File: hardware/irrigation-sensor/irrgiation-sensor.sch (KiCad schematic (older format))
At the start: 35 parts, among them J1 CONUFL001-SMD-T, J2 SHF-105-01-L-D-TH, Q1 PMV250EPEA, Q2 TSM260P02, U1 24LC32, U2 RFM95W, U3 TLV61225, U4 STM32L412KB

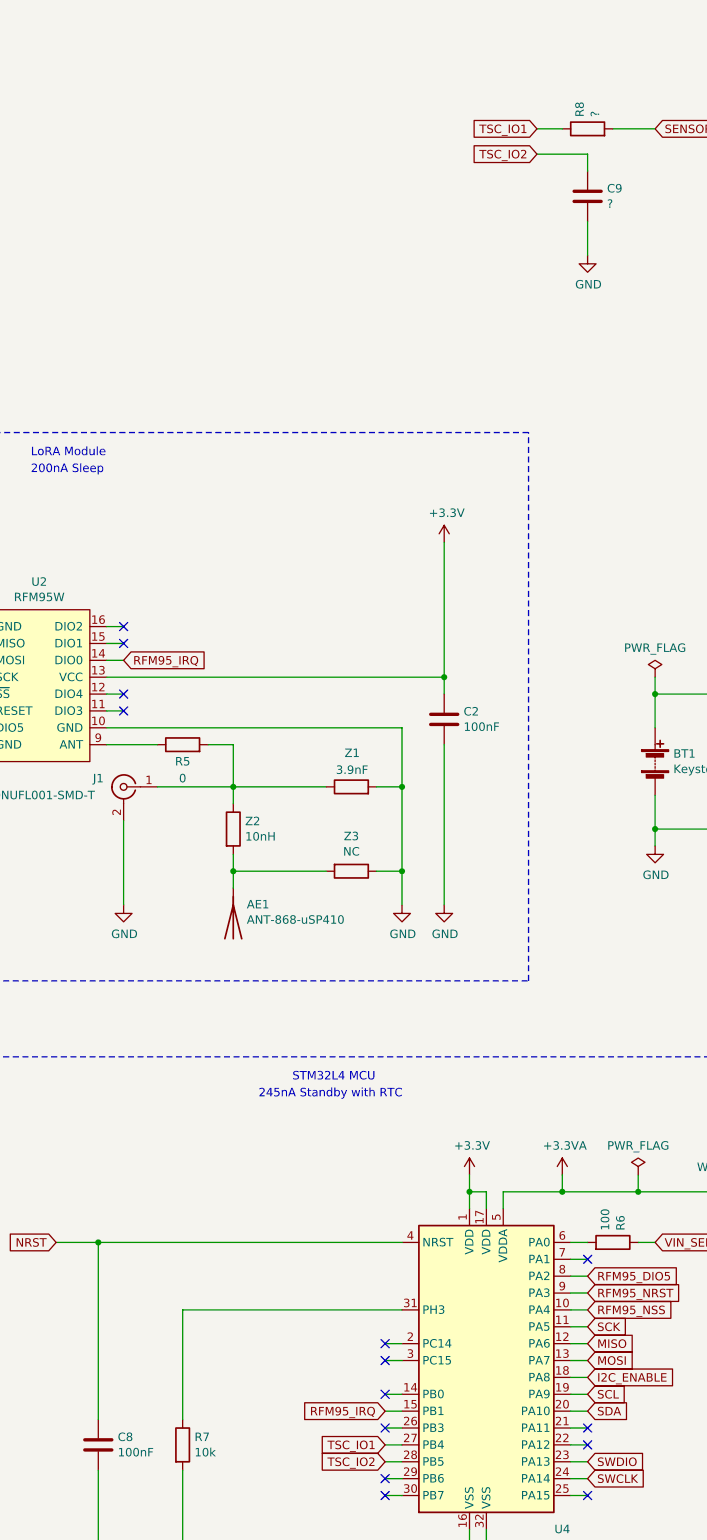
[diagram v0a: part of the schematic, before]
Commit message: PCB revision 2, add data packet handling to climate-sensor
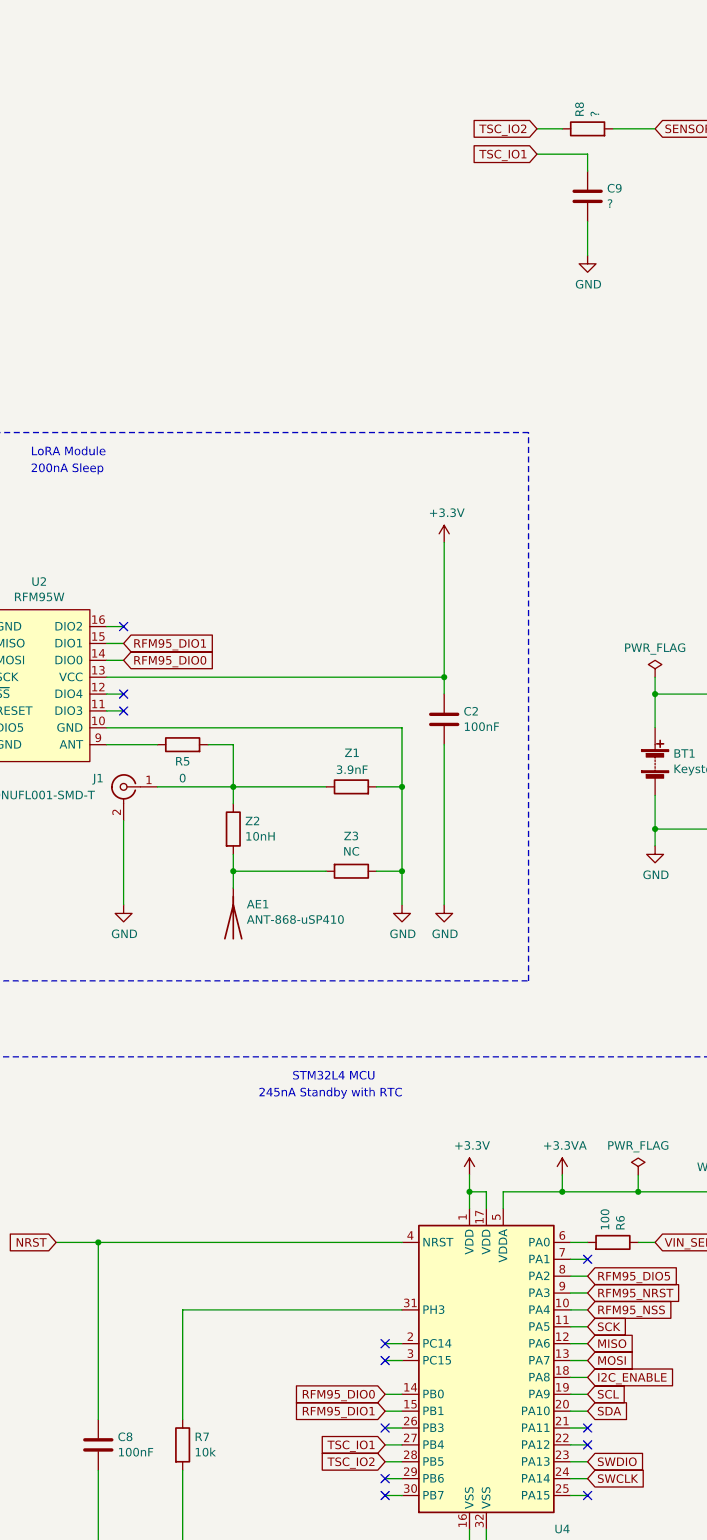
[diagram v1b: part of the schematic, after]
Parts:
- BT1: footprint my-footprints-library:BatteryHolder_Keystone_2462_2xAA_NoSilkscreen -> my-footprints-library:BatteryHolder_Keystone_2468_2xAAA_NoSilkscreen
- H1, H2, H3: footprint MountingHole:MountingHole_3.2mm_M3 -> MountingHole:MountingHole_2.2mm_M2
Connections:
- net TSC_IO1: now also C9.1; no longer R8.1
- net TSC_IO2: now also R8.1; no longer C9.1
- net RFM95_DIO1: now reaches U2.15 (DIO1)
- net RFM95_DIO1: now also U4.15 (PB1)
- net RFM95_DIO0: now reaches U4.14 (PB0)
- net RFM95_DIO0: now also U2.14 (DIO0)
- removed net RFM95_IRQ: U2.14 (DIO0), U4.15 (PB1)
- no-connect marks 16 -> 14
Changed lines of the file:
@@
 F 0 "BT1" H 6408 5646 50  0000 L CNN
 F 1 "Keystone-2462" H 6408 5555 50  0000 L CNN
-F 2 "my-footprints-library:BatteryHolder_Keystone_2462_2xAA_NoSilkscreen" V 6300 5660 50  0001 C CNN
+F 2 "my-footprints-library:BatteryHolder_Keystone_2468_2xAAA_NoSilkscreen" V 6300 5660 50  0001 C CNN
 F 3 "~" V 6300 5660 50  0001 C CNN
 F 4 "2462" H 6300 5600 50  0001 C CNN "#manf"
@@
 	3050 5400 4800 5400
 NoConn ~ 3150 4800
-NoConn ~ 3150 4900
 NoConn ~ 3150 5200
 NoConn ~ 3150 5300
@@
 $EndComp
 Text GLabel 3150 5000 2    50   Input ~ 0
-RFM95_IRQ
+RFM95_DIO0
 Wire Wire Line
 	1550 5400 2250 5400
@@
 Wire Wire Line
 	4800 5400 4800 5750
-Text GLabel 4700 9450 0    50   Input ~ 0
-RFM95_IRQ
+Text GLabel 4700 9350 0    50   Input ~ 0
+RFM95_DIO0
 Text GLabel 5900 8650 2    50   Input ~ 0
 RFM95_DIO5
@@
 Text GLabel 5900 8850 2    50   Input ~ 0
 RFM95_NSS
-Wire Wire Line
-	5800 8450 5900 8450
 $Comp
 L power:PWR_FLAG #FLG0101
@@
 NoConn ~ 5900 9550
 NoConn ~ 5900 9650
-NoConn ~ 4700 9350
 $Comp
 L Device:R R5
@@
 F 0 "H1" H 12800 4896 50  0000 L CNN
 F 1 "MountingHole" H 12800 4805 50  0000 L CNN
-F 2 "MountingHole:MountingHole_3.2mm_M3" H 12700 4850 50  0001 C CNN
+F 2 "MountingHole:MountingHole_2.2mm_M2" H 12700 4850 50  0001 C CNN
 F 3 "~" H 12700 4850 50  0001 C CNN
 	1    12700 4850
-	1    0    0    -1
-$EndComp
-$Comp
-L Mechanical:MountingHole H2
-U 1 1 61711343
-P 12700 5100
-F 0 "H2" H 12800 5146 50  0000 L CNN
-F 1 "MountingHole" H 12800 5055 50  0000 L CNN
-F 2 "MountingHole:MountingHole_3.2mm_M3" H 12700 5100 50  0001 C CNN
-F 3 "~" H 12700 5100 50  0001 C CNN
-	1    12700 5100
 	1    0    0    -1
 $EndComp
@@
 F 0 "H3" H 12800 5396 50  0000 L CNN
 F 1 "MountingHole" H 12800 5305 50  0000 L CNN
-F 2 "MountingHole:MountingHole_3.2mm_M3" H 12700 5350 50  0001 C CNN
+F 2 "MountingHole:MountingHole_2.2mm_M2" H 12700 5350 50  0001 C CNN
 F 3 "~" H 12700 5350 50  0001 C CNN
 	1    12700 5350
@@
 Text GLabel 4700 9650 0    50   Input ~ 0
 TSC_IO1
-Text GLabel 5600 1850 0    50   Input ~ 0
+Text GLabel 5600 2000 0    50   Input ~ 0
 TSC_IO1
 $Comp
@@
 Wire Wire Line
 	5900 2400 5900 2600
-Text GLabel 5600 2000 0    50   Input ~ 0
+Text GLabel 5600 1850 0    50   Input ~ 0
 TSC_IO2
 Text GLabel 6300 1850 2    50   Input ~ 0
@@
 Wire Wire Line
 	8000 5200 8800 5200
+Text GLabel 3150 4900 2    50   Input ~ 0
+RFM95_DIO1
+Wire Wire Line
+	5900 8450 5800 8450
+Text GLabel 4700 9450 0    50   Input ~ 0
+RFM95_DIO1
+$Comp
+L Mechanical:MountingHole H2
+U 1 1 61E00267
+P 12700 5100
+F 0 "H2" H 12800 5146 50  0000 L CNN
+F 1 "MountingHole" H 12800 5055 50  0000 L CNN
+F 2 "MountingHole:MountingHole_2.2mm_M2" H 12700 5100 50  0001 C CNN
+F 3 "~" H 12700 5100 50  0001 C CNN
+	1    12700 5100
+	1    0    0    -1
+$EndComp
 $EndSCHEMATC

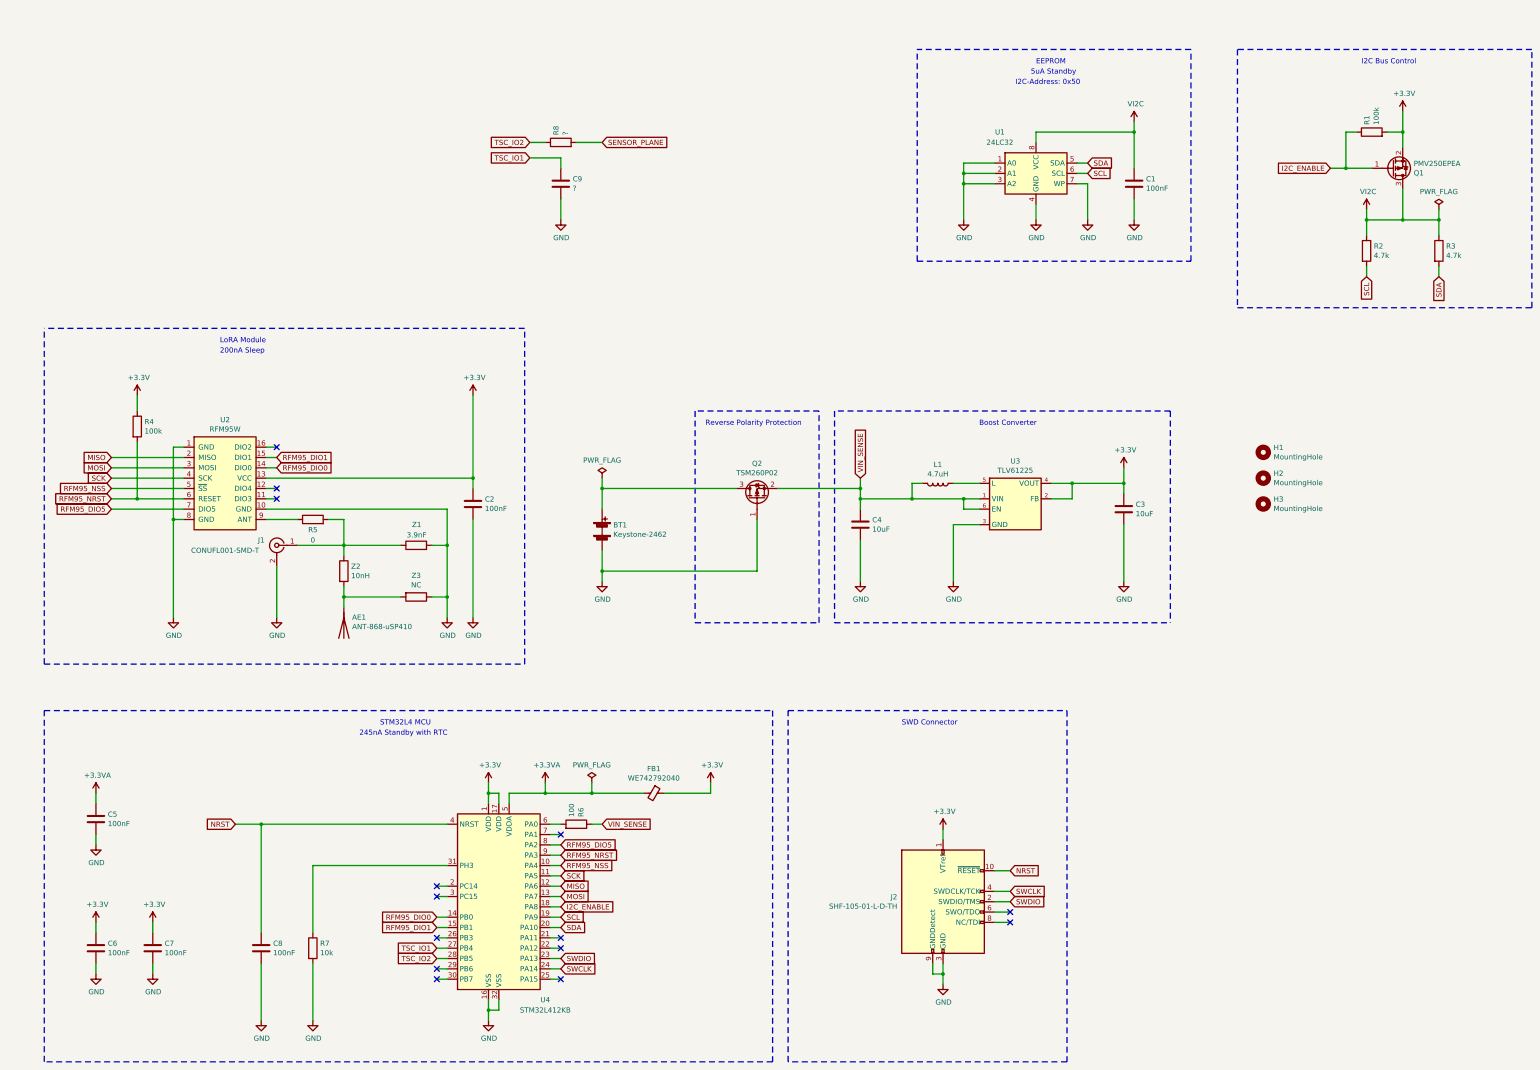
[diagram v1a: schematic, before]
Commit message: Implement user management and authorization
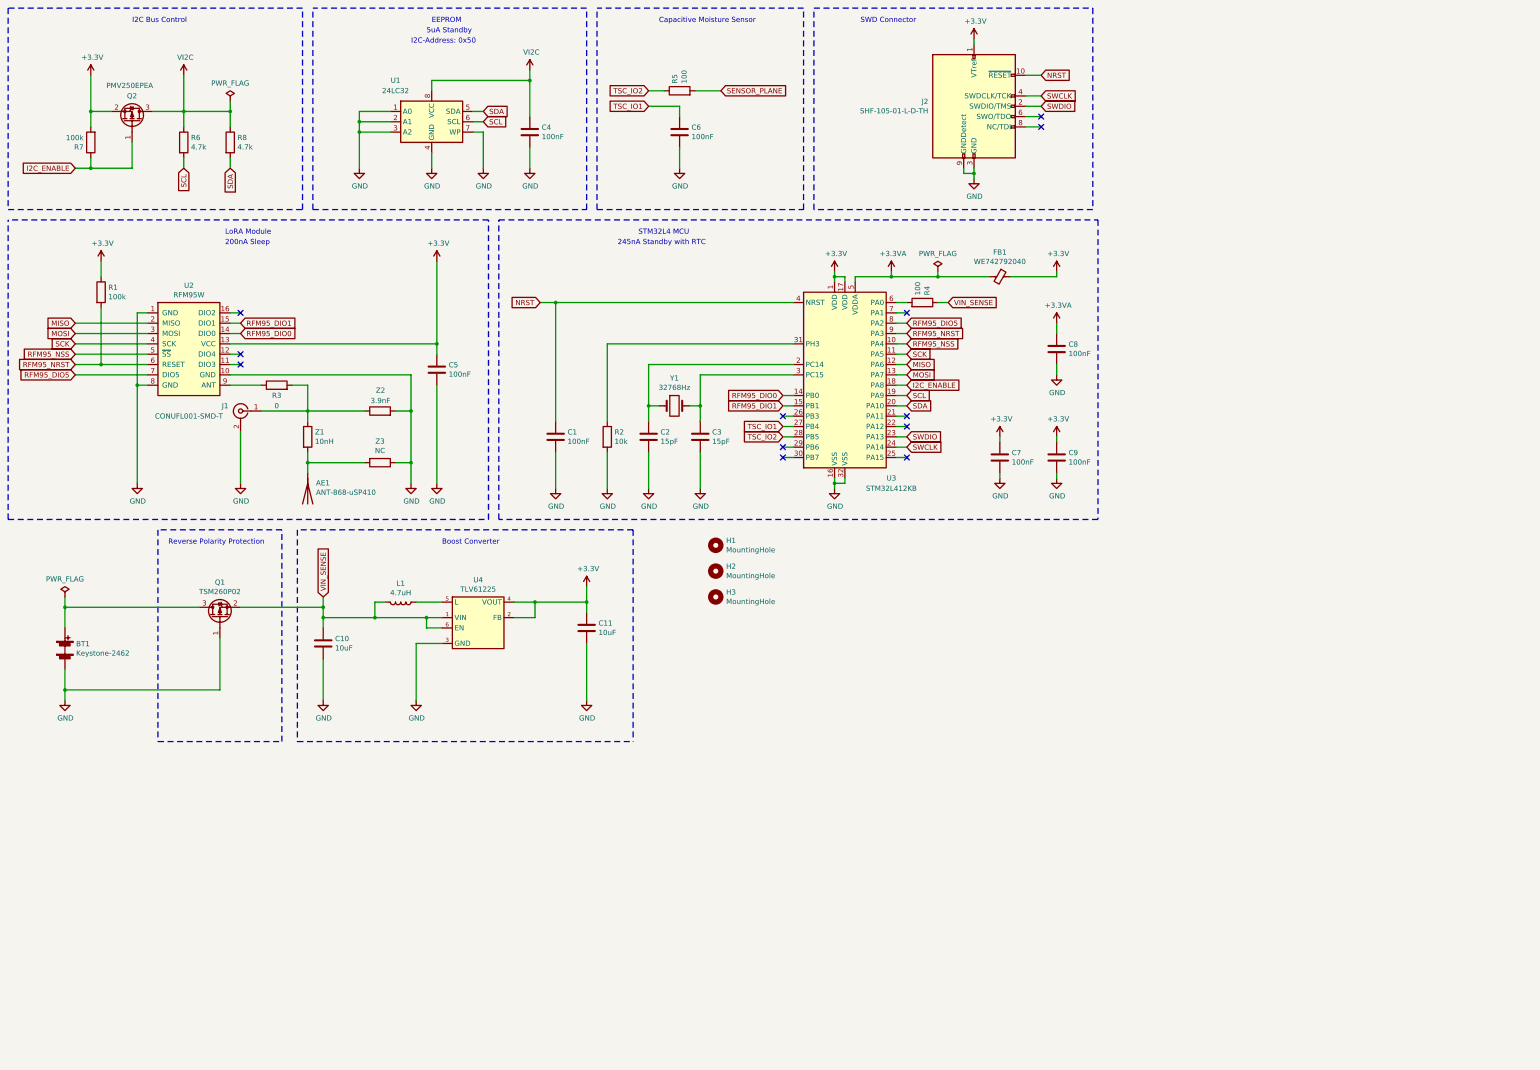
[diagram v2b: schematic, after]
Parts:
- added C2, C3: 15pF, Capacitor_SMD:C_0805_2012Metric_Pad1.18x1.45mm_HandSolder, symbol Device:C
- added Y1: 32768Hz, Crystal:Crystal_SMD_EuroQuartz_EQ161-2Pin_3.2x1.5mm_HandSoldering, symbol Device:Crystal
- C6: renamed from C9; value ? -> 100nF
- R5: renamed from R8; value ? -> 100
- renumbered C8 to C1, C4 to C10, C3 to C11, C1 to C4, C2 to C5, C6 to C7, C5 to C8, C7 to C9, Q2 to Q1, Q1 to Q2, R4 to R1, R7 to R2, R5 to R3, R6 to R4, R2 to R6, R1 to R7, R3 to R8, U4 to U3, U3 to U4, Z2 to Z1, Z1 to Z2
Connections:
- net GND: now also C2.2, C3.2
- net at U3.2 (PC14): now also C2.1, Y1.1
- net at U3.3 (PC15): now also C3.1, Y1.2
- no-connect marks 14 -> 12
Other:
- note added: "Capacitive Moisture Sensor"
- moved on the sheet: AE1, BT1, C1, C10, C11, C4, C5, C6, C7, C8, C9, FB1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

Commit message: Implement downlink functionality
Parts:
- Z1: value 10nH -> 11nH
- Z2: value 3.9nF -> NC
- Z3: value NC -> 900fF
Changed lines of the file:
@@
 P 3450 4700
 F 0 "Z1" H 3520 4746 50  0000 L CNN
-F 1 "10nH" H 3520 4655 50  0000 L CNN
+F 1 "11nH" H 3520 4655 50  0000 L CNN
 F 2 "Resistor_SMD:R_0805_2012Metric_Pad1.20x1.40mm_HandSolder" V 3380 4700 50  0001 C CNN
 F 3 "~" H 3450 4700 50  0001 C CNN
@@
 P 4150 4450
 F 0 "Z2" V 4350 4400 50  0000 L CNN
-F 1 "3.9nF" V 4250 4350 50  0000 L CNN
+F 1 "NC" V 4250 4350 50  0000 L CNN
 F 2 "Resistor_SMD:R_0805_2012Metric_Pad1.20x1.40mm_HandSolder" V 4080 4450 50  0001 C CNN
 F 3 "~" H 4150 4450 50  0001 C CNN
@@
 P 4150 4950
 F 0 "Z3" V 3943 4950 50  0000 C CNN
-F 1 "NC" V 4034 4950 50  0000 C CNN
+F 1 "900fF" V 4034 4950 50  0000 C CNN
 F 2 "Resistor_SMD:R_0805_2012Metric_Pad1.20x1.40mm_HandSolder" V 4080 4950 50  0001 C CNN
 F 3 "~" H 4150 4950 50  0001 C CNN

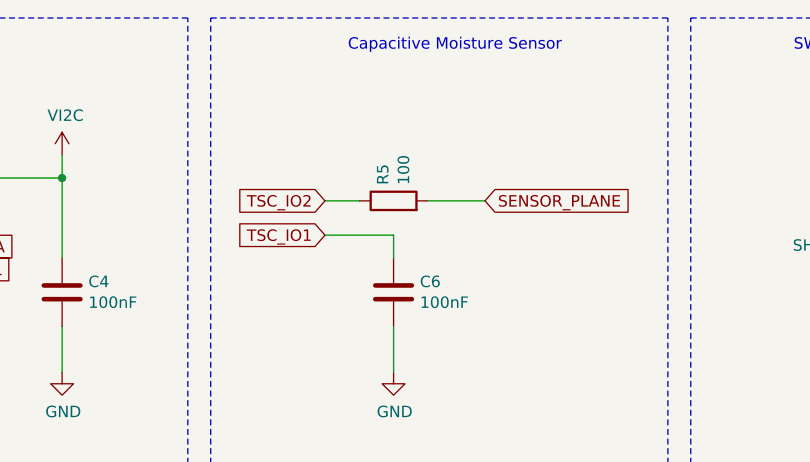
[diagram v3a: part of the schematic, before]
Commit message: Add different irrigation sensor hardware revisions and cypress e2e tests
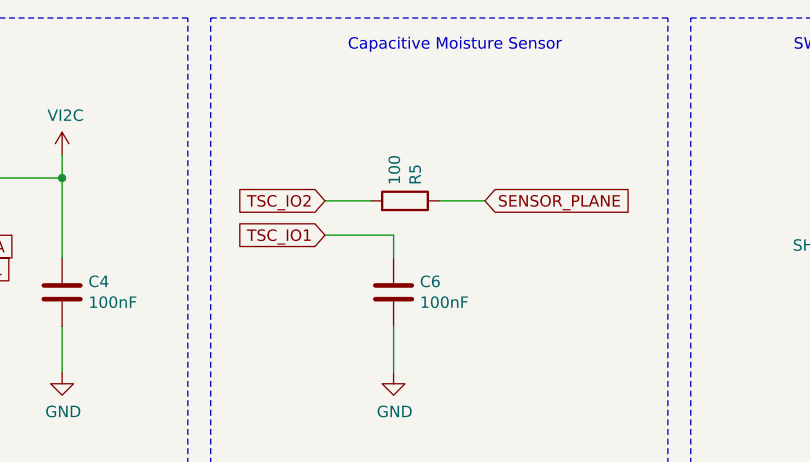
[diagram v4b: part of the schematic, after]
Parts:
- R5: #manf RC0805FR-074K7L -> RC0805FR-07100RL; digikey# 311-4.70KCRCT-ND -> 311-100CRCT-ND; mouser# 603-RC0805FR-074K7L -> 603-RC0805FR-07100RL
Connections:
- net SENSOR_PLANE: now also R5.1; no longer R5.2
- net TSC_IO2: now also R5.2; no longer R5.1
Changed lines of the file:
@@
 	1    0    0    -1
 $EndComp
-$Comp
-L Device:R R5
-U 1 1 61B6AB8D
-P 7050 1350
-F 0 "R5" H 7120 1396 50  0000 L CNN
-F 1 "100" H 7120 1305 50  0000 L CNN
-F 2 "Resistor_SMD:R_0805_2012Metric_Pad1.20x1.40mm_HandSolder" V 6980 1350 50  0001 C CNN
-F 3 "~" H 7050 1350 50  0001 C CNN
-F 4 "RC0805FR-074K7L" H 7050 1350 50  0001 C CNN "#manf"
-F 5 "311-4.70KCRCT-ND" H 7050 1350 50  0001 C CNN "digikey#"
-F 6 "603-RC0805FR-074K7L" H 7050 1350 50  0001 C CNN "mouser#"
-	1    7050 1350
-	0    -1   -1   0
-$EndComp
-Wire Wire Line
-	6900 1350 6750 1350
 Wire Wire Line
 	6750 1500 7050 1500
@@
 Text GLabel 7450 1350 2    50   Input ~ 0
 SENSOR_PLANE
-Wire Wire Line
-	7200 1350 7450 1350
 Wire Wire Line
 	2800 6350 3600 6350
@@
 Text Notes 6450 2850 0    50   ~ 0
 245nA Standby with RTC
+$Comp
+L Device:R R5
+U 1 1 622F8A51
+P 7100 1350
+F 0 "R5" H 7170 1396 50  0000 L CNN
+F 1 "100" H 7170 1305 50  0000 L CNN
+F 2 "Resistor_SMD:R_0805_2012Metric_Pad1.20x1.40mm_HandSolder" V 7030 1350 50  0001 C CNN
+F 3 "~" H 7100 1350 50  0001 C CNN
+F 4 "RC0805FR-07100RL" H 7100 1350 50  0001 C CNN "#manf"
+F 5 "311-100CRCT-ND" H 7100 1350 50  0001 C CNN "digikey#"
+F 6 "603-RC0805FR-07100RL" H 7100 1350 50  0001 C CNN "mouser#"
+	1    7100 1350
+	0    1    -1   0
+$EndComp
+Wire Wire Line
+	7250 1350 7450 1350
+Wire Wire Line
+	6750 1350 6950 1350
 $EndSCHEMATC
